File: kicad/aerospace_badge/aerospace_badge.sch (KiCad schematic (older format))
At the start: 19 parts, among them J1 Conn_02x03_Counter_Clockwise, J2 Conn_01x02, J3 Conn_01x01_Male, J4 Conn_01x02, J5 Conn_01x04, J6 Conn_01x01_Male, J7 Conn_01x01_Male, U1 ATtiny85-20SU

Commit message: updated footprints per new datasheets.
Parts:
- D1: footprint sunled:XZDGK45WT-9 -> sunled:XZMYK45WT-9
- D3: footprint sunled:XZDGK45WT-9 -> sunled:XZM2CRK45WT-9
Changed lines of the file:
@@
 Sheet 1 1
 Title "Aerospace Village Badge 2020"
-Date "2020-06-15"
+Date "2020-06-17"
 Rev "v02"
 Comp ""
@@
 F 0 "D1" V 6889 4332 50  0000 R CNN
 F 1 "LED" V 6798 4332 50  0000 R CNN
-F 2 "sunled:XZDGK45WT-9" H 6850 4450 50  0001 C CNN
+F 2 "sunled:XZMYK45WT-9" H 6850 4450 50  0001 C CNN
 F 3 "~" H 6850 4450 50  0001 C CNN
 	1    6850 4450
@@
 F 0 "D3" H 7293 3167 50  0000 C CNN
 F 1 "LED" H 7293 3076 50  0000 C CNN
-F 2 "sunled:XZDGK45WT-9" H 7300 2950 50  0001 C CNN
+F 2 "sunled:XZM2CRK45WT-9" H 7300 2950 50  0001 C CNN
 F 3 "~" H 7300 2950 50  0001 C CNN
 	1    7300 2950

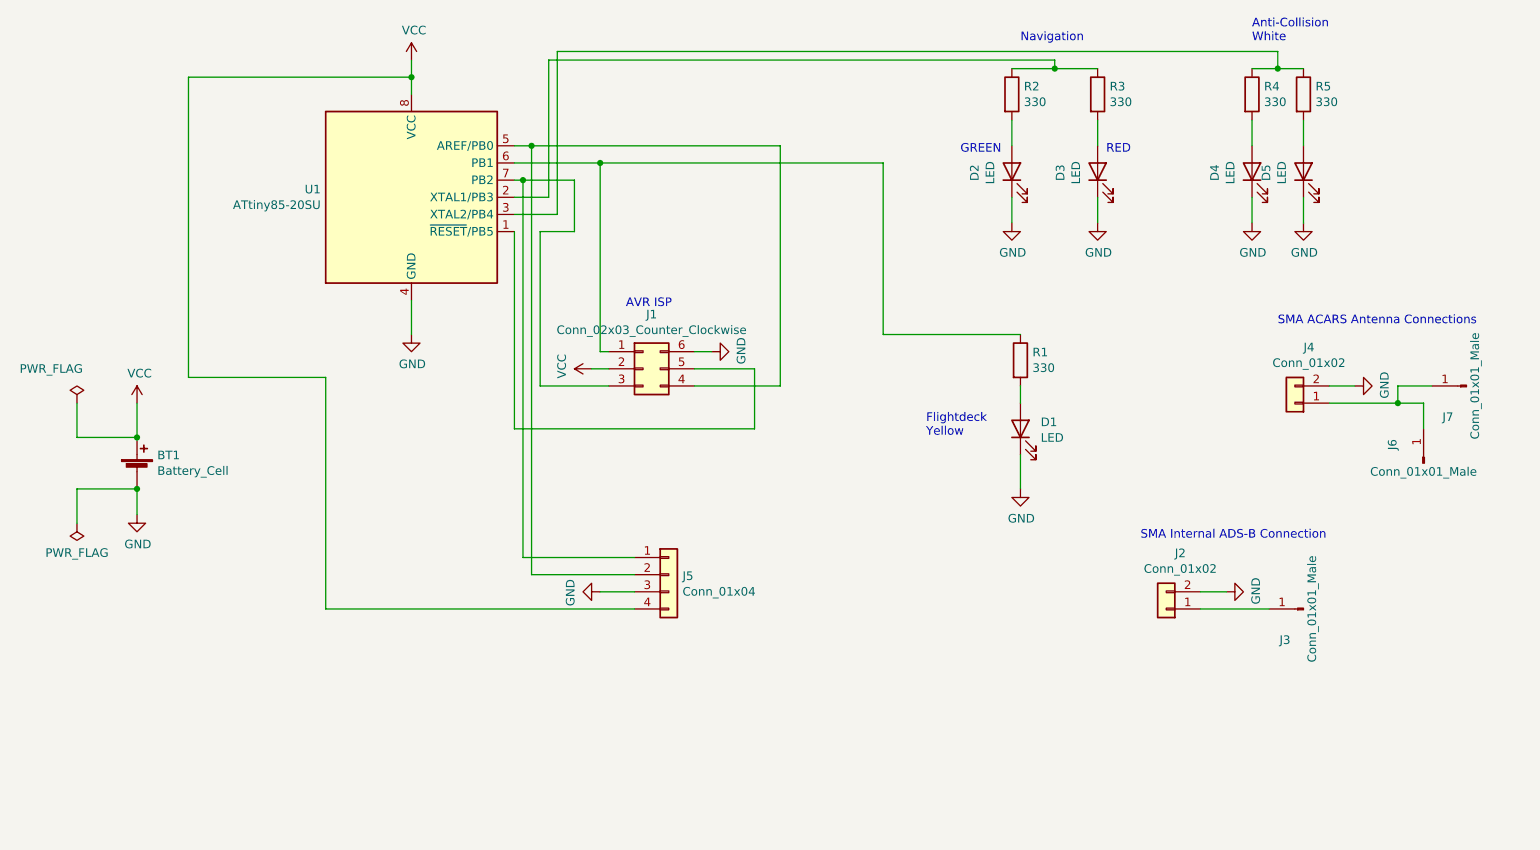
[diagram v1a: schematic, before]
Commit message: updated, needs another check prior to fabrication.
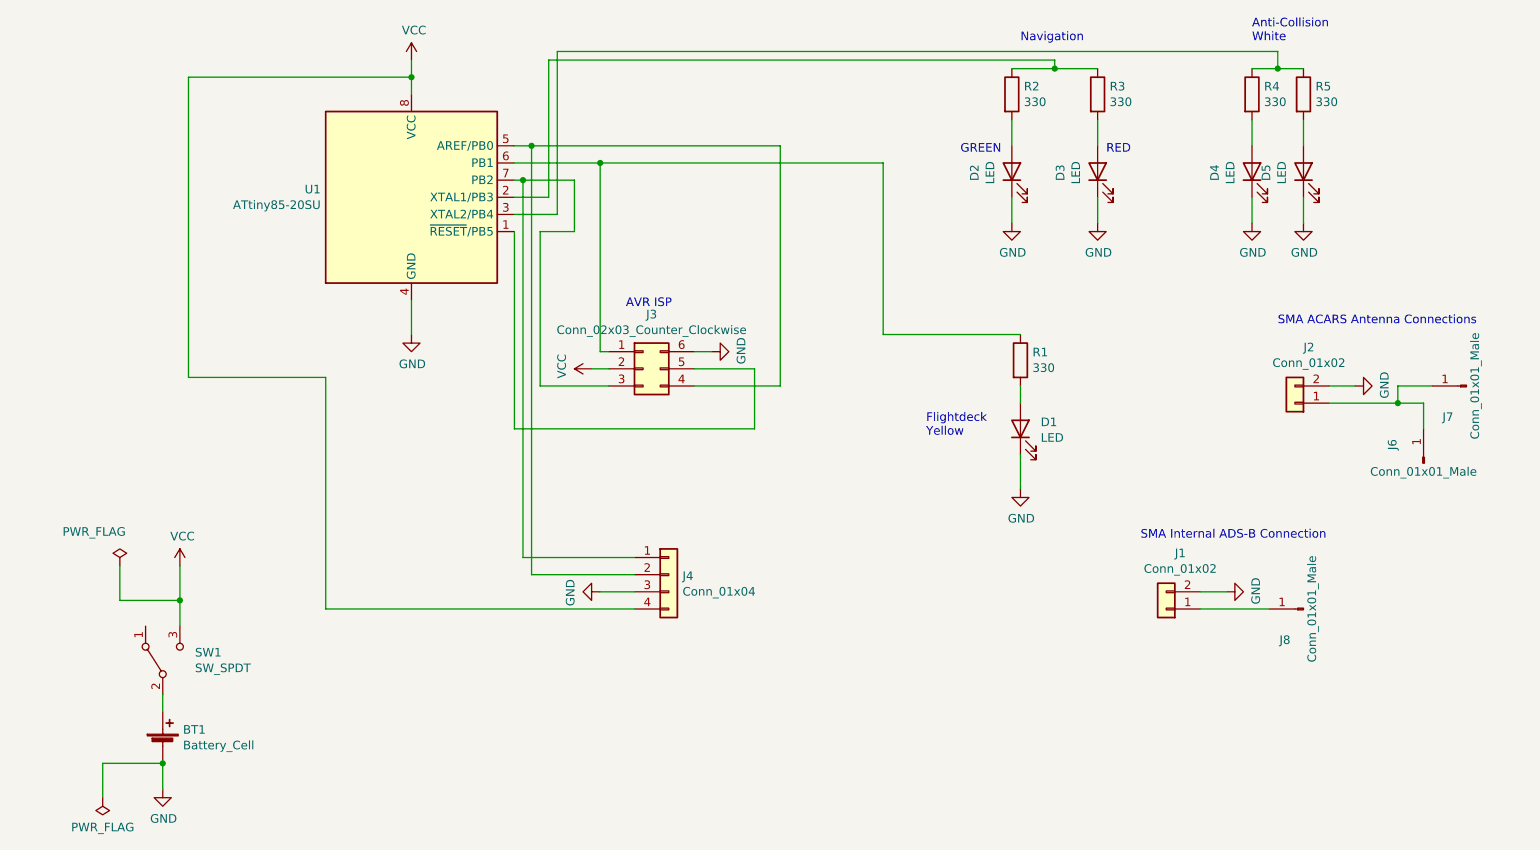
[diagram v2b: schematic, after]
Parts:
- added SW1: SW_SPDT, aerospace_badge:switch_JS202011SCQN, symbol Switch:SW_SPDT
- J8: renamed from J3; footprint aerospace_badge:badge -> aerospace_badge:badge_v02
- renumbered J2 to J1, J4 to J2, J1 to J3, J5 to J4
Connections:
- net VCC: now also SW1.3 (C); no longer BT1.1 (+)
- new net: BT1.1 (+), SW1.2 (B)
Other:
- moved on the sheet: BT1
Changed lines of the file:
@@
 $EndComp
 $Comp
-L Connector_Generic:Conn_02x03_Counter_Clockwise J1
+L Connector_Generic:Conn_02x03_Counter_Clockwise J3
 U 1 1 5EDBBBF4
 P 4650 4100
-F 0 "J1" H 4700 4417 50  0000 C CNN
+F 0 "J3" H 4700 4417 50  0000 C CNN
 F 1 "Conn_02x03_Counter_Clockwise" H 4700 4326 50  0000 C CNN
 F 2 "aerospace_badge:isp_pad" H 4650 4100 50  0001 C CNN
@@
 L Device:Battery_Cell BT1
 U 1 1 5EDBC3F4
-P 1700 4700
-F 0 "BT1" H 1818 4796 50  0000 L CNN
-F 1 "Battery_Cell" H 1818 4705 50  0000 L CNN
-F 2 "Battery:BatteryHolder_Keystone_3034_1x20mm" V 1700 4760 50  0001 C CNN
-F 3 "~" V 1700 4760 50  0001 C CNN
-	1    1700 4700
+P 1850 6300
+F 0 "BT1" H 1968 6396 50  0000 L CNN
+F 1 "Battery_Cell" H 1968 6305 50  0000 L CNN
+F 2 "Battery:BatteryHolder_Keystone_3034_1x20mm" V 1850 6360 50  0001 C CNN
+F 3 "~" V 1850 6360 50  0001 C CNN
+	1    1850 6300
 	1    0    0    -1
 $EndComp
@@
 $EndComp
 $Comp
-L Connector:Conn_01x01_Male J3
+L Connector:Conn_01x01_Male J8
 U 1 1 5EDBD76D
 P 8500 5500
-F 0 "J3" H 8608 5681 50  0000 C CNN
+F 0 "J8" H 8608 5681 50  0000 C CNN
 F 1 "Conn_01x01_Male" V 8450 5500 50  0000 C CNN
-F 2 "aerospace_badge:badge" H 8500 5500 50  0001 C CNN
+F 2 "aerospace_badge:badge_v02" H 8500 5500 50  0001 C CNN
 F 3 "~" H 8500 5500 50  0001 C CNN
 	1    8500 5500
@@
 L power:GND #PWR0105
 U 1 1 5EDFF512
-P 1700 4950
-F 0 "#PWR0105" H 1700 4700 50  0001 C CNN
-F 1 "GND" H 1705 4777 50  0000 C CNN
-F 2 "" H 1700 4950 50  0001 C CNN
-F 3 "" H 1700 4950 50  0001 C CNN
-	1    1700 4950
-	1    0    0    -1
-$EndComp
-$Comp
-L Connector_Generic:Conn_01x02 J2
+P 1850 6550
+F 0 "#PWR0105" H 1850 6300 50  0001 C CNN
+F 1 "GND" H 1855 6377 50  0000 C CNN
+F 2 "" H 1850 6550 50  0001 C CNN
+F 3 "" H 1850 6550 50  0001 C CNN
+	1    1850 6550
+	1    0    0    -1
+$EndComp
+$Comp
+L Connector_Generic:Conn_01x02 J1
 U 1 1 5EE05FC3
 P 7700 5500
-F 0 "J2" H 7618 5175 50  0000 C CNN
+F 0 "J1" H 7618 5175 50  0000 C CNN
 F 1 "Conn_01x02" H 7618 5266 50  0000 C CNN
 F 2 "aerospace_badge:linx_sma_jack_female_socket" H 7700 5500 50  0001 C CNN
@@
 	6800 3100 6800 3250
 Wire Wire Line
-	1700 4800 1700 4950
+	1850 6400 1850 6550
 $Comp
 L power:PWR_FLAG #FLG0101
 U 1 1 5EDE2277
-P 1350 4300
-F 0 "#FLG0101" H 1350 4375 50  0001 C CNN
-F 1 "PWR_FLAG" H 1200 4500 50  0000 C CNN
-F 2 "" H 1350 4300 50  0001 C CNN
-F 3 "~" H 1350 4300 50  0001 C CNN
-	1    1350 4300
-	1    0    0    -1
-$EndComp
-Wire Wire Line
-	1350 4500 1350 4300
-Connection ~ 1700 4500
-Wire Wire Line
-	1700 4500 1700 4300
+P 1600 5250
+F 0 "#FLG0101" H 1600 5325 50  0001 C CNN
+F 1 "PWR_FLAG" H 1450 5450 50  0000 C CNN
+F 2 "" H 1600 5250 50  0001 C CNN
+F 3 "~" H 1600 5250 50  0001 C CNN
+	1    1600 5250
+	1    0    0    -1
+$EndComp
+Wire Wire Line
+	1600 5450 1600 5250
+Wire Wire Line
+	1950 5450 1950 5250
 $Comp
 L power:VCC #PWR0106
 U 1 1 5EE0042C
-P 1700 4300
-F 0 "#PWR0106" H 1700 4150 50  0001 C CNN
-F 1 "VCC" H 1715 4473 50  0000 C CNN
-F 2 "" H 1700 4300 50  0001 C CNN
-F 3 "" H 1700 4300 50  0001 C CNN
-	1    1700 4300
+P 1950 5250
+F 0 "#PWR0106" H 1950 5100 50  0001 C CNN
+F 1 "VCC" H 1965 5423 50  0000 C CNN
+F 2 "" H 1950 5250 50  0001 C CNN
+F 3 "" H 1950 5250 50  0001 C CNN
+	1    1950 5250
 	1    0    0    -1
 $EndComp
@@
 L power:PWR_FLAG #FLG0102
 U 1 1 5EDE36CB
-P 1350 5000
-F 0 "#FLG0102" H 1350 5075 50  0001 C CNN
-F 1 "PWR_FLAG" H 1350 5173 50  0000 C CNN
-F 2 "" H 1350 5000 50  0001 C CNN
-F 3 "~" H 1350 5000 50  0001 C CNN
-	1    1350 5000
+P 1500 6600
+F 0 "#FLG0102" H 1500 6675 50  0001 C CNN
+F 1 "PWR_FLAG" H 1500 6773 50  0000 C CNN
+F 2 "" H 1500 6600 50  0001 C CNN
+F 3 "~" H 1500 6600 50  0001 C CNN
+	1    1500 6600
 	-1   0    0    1
 $EndComp
 Wire Wire Line
-	1700 4800 1350 4800
-Wire Wire Line
-	1350 4800 1350 5000
-Connection ~ 1700 4800
-Wire Wire Line
-	1350 4500 1700 4500
-$Comp
-L Connector_Generic:Conn_01x02 J4
+	1850 6400 1500 6400
+Wire Wire Line
+	1500 6400 1500 6600
+Wire Wire Line
+	1600 5450 1950 5450
+$Comp
+L Connector_Generic:Conn_01x02 J2
 U 1 1 5EDC5AF4
 P 8450 4300
-F 0 "J4" H 8368 3975 50  0000 C CNN
+F 0 "J2" H 8368 3975 50  0000 C CNN
 F 1 "Conn_01x02" H 8368 4066 50  0000 C CNN
 F 2 "aerospace_badge:linx_sma_jack_female_socket" H 8450 4300 50  0001 C CNN
@@
 SMA ACARS Antenna Connections
 $Comp
-L Connector_Generic:Conn_01x04 J5
+L Connector_Generic:Conn_01x04 J4
 U 1 1 5EEA3870
 P 4800 5300
-F 0 "J5" H 4880 5292 50  0000 L CNN
+F 0 "J4" H 4880 5292 50  0000 L CNN
 F 1 "Conn_01x04" H 4880 5201 50  0000 L CNN
 F 2 "Connector_PinHeader_2.54mm:PinHeader_1x04_P2.54mm_Vertical" H 4800 5300 50  0001 C CNN
@@
 Text Notes 6500 2850 0    50   ~ 0
 GREEN
+$Comp
+L Switch:SW_SPDT SW1
+U 1 1 5EF0E98B
+P 1850 5800
+F 0 "SW1" V 1896 5612 50  0000 R CNN
+F 1 "SW_SPDT" V 1805 5612 50  0000 R CNN
+F 2 "aerospace_badge:switch_JS202011SCQN" H 1850 5800 50  0001 C CNN
+F 3 "~" H 1850 5800 50  0001 C CNN
+	1    1850 5800
+	0    -1   -1   0
+$EndComp
+Connection ~ 1850 6400
+Wire Wire Line
+	1850 6100 1850 6000
+Wire Wire Line
+	1950 5600 1950 5450
+Connection ~ 1950 5450
 $EndSCHEMATC
